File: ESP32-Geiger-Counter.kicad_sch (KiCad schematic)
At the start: 25 parts, among them J1 USB_C_Receptacle_USB2.0_16P, U1 TP4056-42-ESOP8, U2 ESP32-WROOM-32, U3 CP2102N-Axx-xQFN20, U4 TPS63031DSK

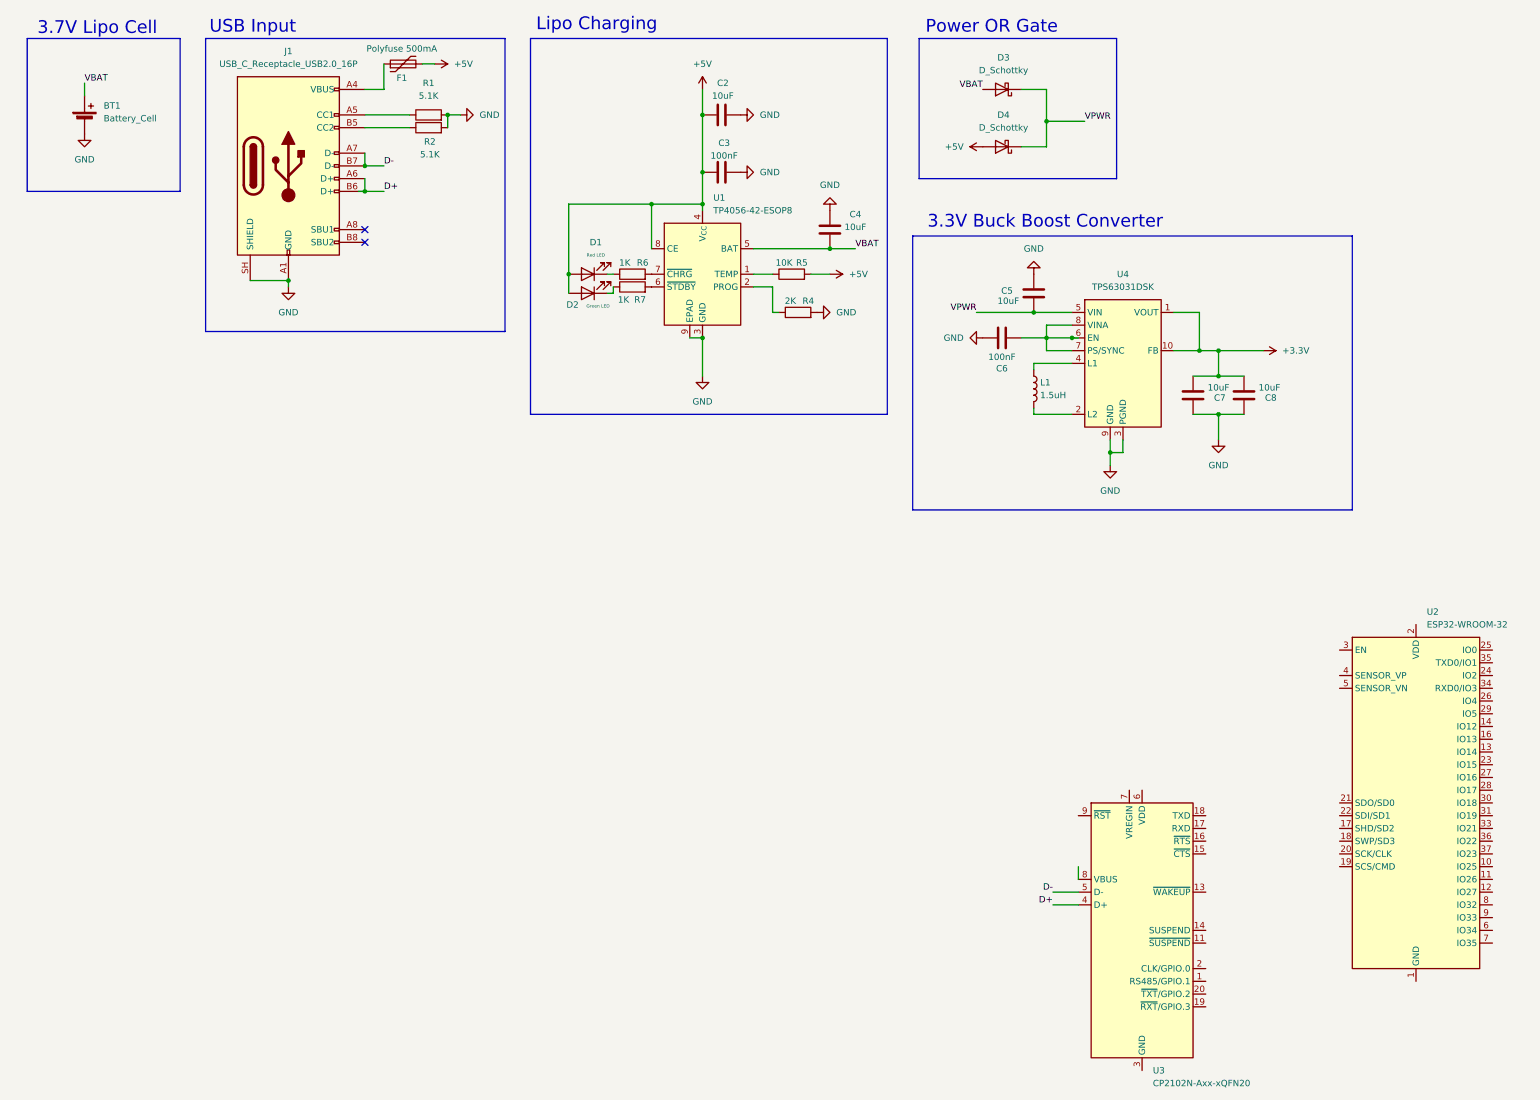
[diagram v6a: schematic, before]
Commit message: added tvs diode array and inrush bulk cap for usb
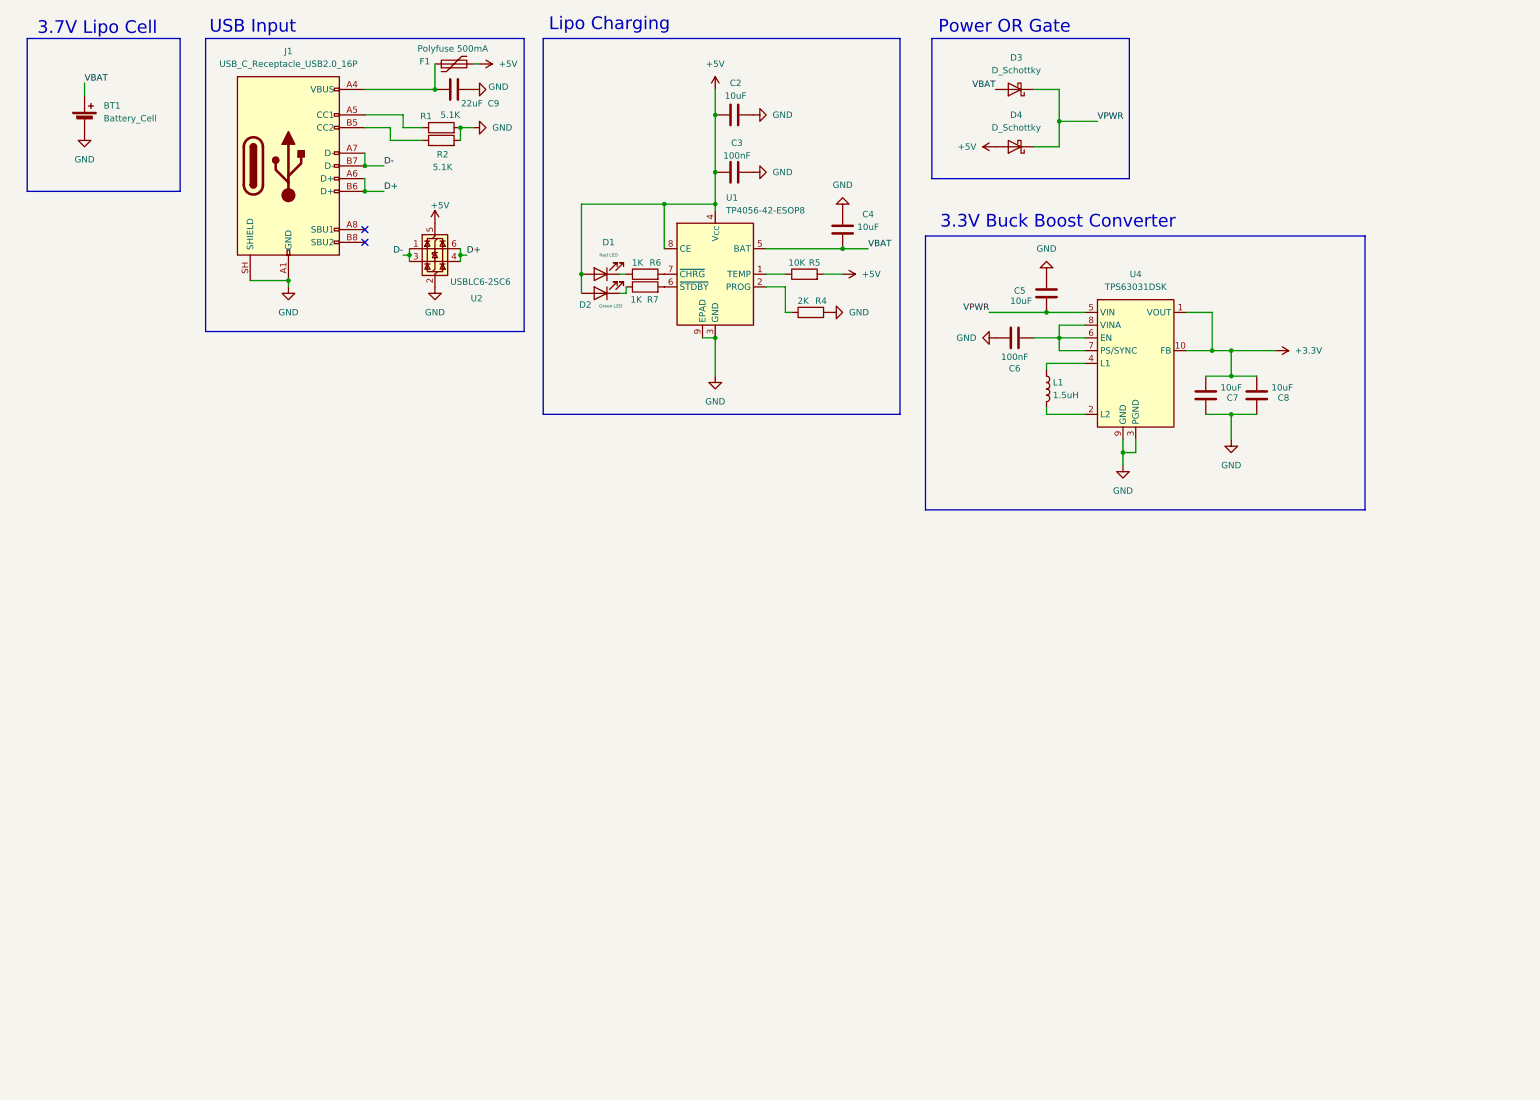
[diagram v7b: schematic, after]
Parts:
- removed U2: ESP32-WROOM-32, RF_Module:ESP32-WROOM-32, symbol RF_Module:ESP32-WROOM-32
- removed U3: CP2102N-Axx-xQFN20, Package_DFN_QFN:SiliconLabs_QFN-20-1EP_3x3mm_P0.5mm, symbol Interface_USB:CP2102N-Axx-xQFN20
- added C9: 22uF, symbol Device:C
- added U2: USBLC6-2SC6, Package_TO_SOT_SMD:SOT-23-6, symbol Power_Protection:USBLC6-2SC6
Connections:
- net +5V: now also U2.5 (VBUS)
- net D+: now also U2.4 (I/O2), U2.6 (I/O1)
- net D-: now also U2.1 (I/O1), U2.3 (I/O2)
- net GND: now also C9.1, U2.2 (GND)
- net at F1.1, J1.A4 (VBUS), J1.A9 (VBUS)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: now also C9.2
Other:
- moved on the sheet: C2, C3, C4, C5, C6, C7, C8, D1, D2, D3, D4, F1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

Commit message: big updates
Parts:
- added C10: 100nF, symbol Device:C
- added R3: 22K, symbol Device:R
- added R8: 47K, symbol Device:R
- added R9: 10K, symbol Device:R
- added U3: ESP32-WROOM-32, RF_Module:ESP32-WROOM-32, symbol RF_Module:ESP32-WROOM-32
- added U5: CP2102N-Axx-xQFN20, Package_DFN_QFN:SiliconLabs_QFN-20-1EP_3x3mm_P0.5mm_EP1.8x1.8mm, symbol Interface_USB:CP2102N-Axx-xQFN20
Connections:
- net +3.3V: now also C10.2, R9.2, U3.2 (VDD), U5.6 (VDD)
- net +5V: now also R3.1, U5.7 (VREGIN)
- net D+: now also U5.4 (D+)
- net D-: now also U5.5 (D-)
- net GND: now also C10.1, R8.2, U3.1 (GND), U3.15 (GND), U3.38 (GND), U3.39 (GND), U5.12 (GND), U5.21 (GND), U5.3 (GND)
- new net: R3.2, R8.1, U5.8 (VBUS)
- new net: R9.1, U5.9 (~{RST})
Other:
- moved on the sheet: C9, F1
